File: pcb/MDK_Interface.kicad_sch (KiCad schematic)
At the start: 14 parts, among them J1 GROVE-CONNECTOR-DIP_4P-2.0_, J10 Conn_01x02, J11 Conn_01x02, J2 GROVE-CONNECTOR-DIP-90D_4P-2.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, J3 GROVE-CONNECTOR-DIP_4P-2.0_, J4 GROVE-CONNECTOR-DIP_4P-2.0_, J5 GROVE-CONNECTOR-DIP_4P-2.0_, J6 GROVE-CONNECTOR-DIP_4P-2.0_, J7 seeed:GROVE-HW4-2.0, J8 GROVE-CONNECTOR-SMD_4+2P-2.0_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

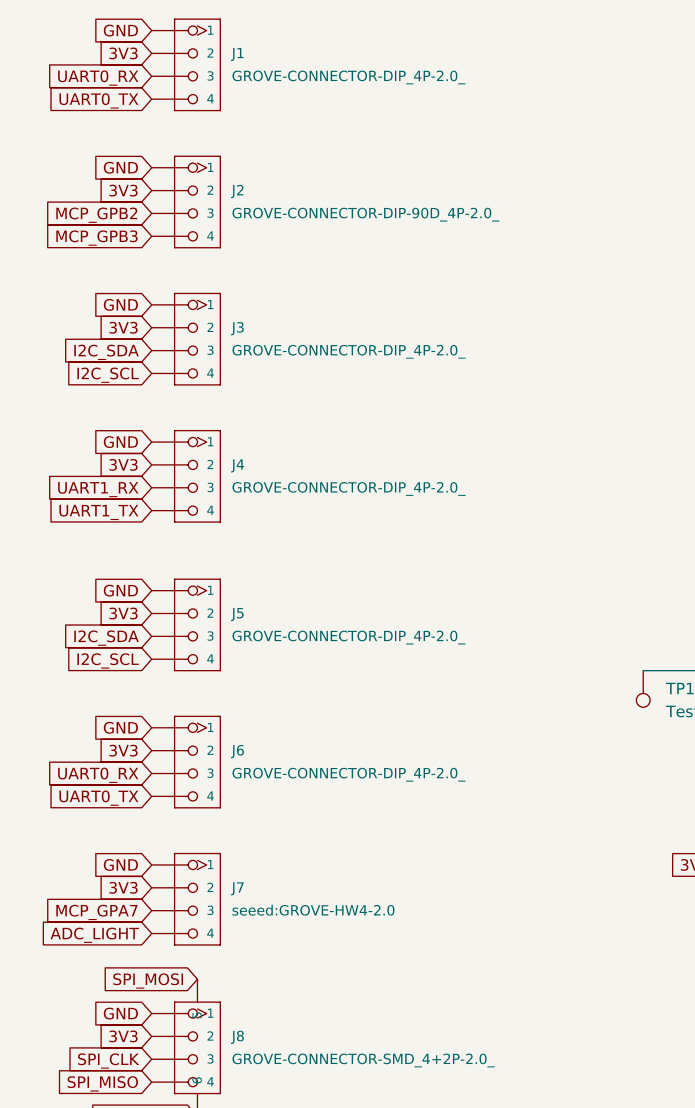
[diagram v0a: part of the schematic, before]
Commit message: adds grove connectors fix and rerouting
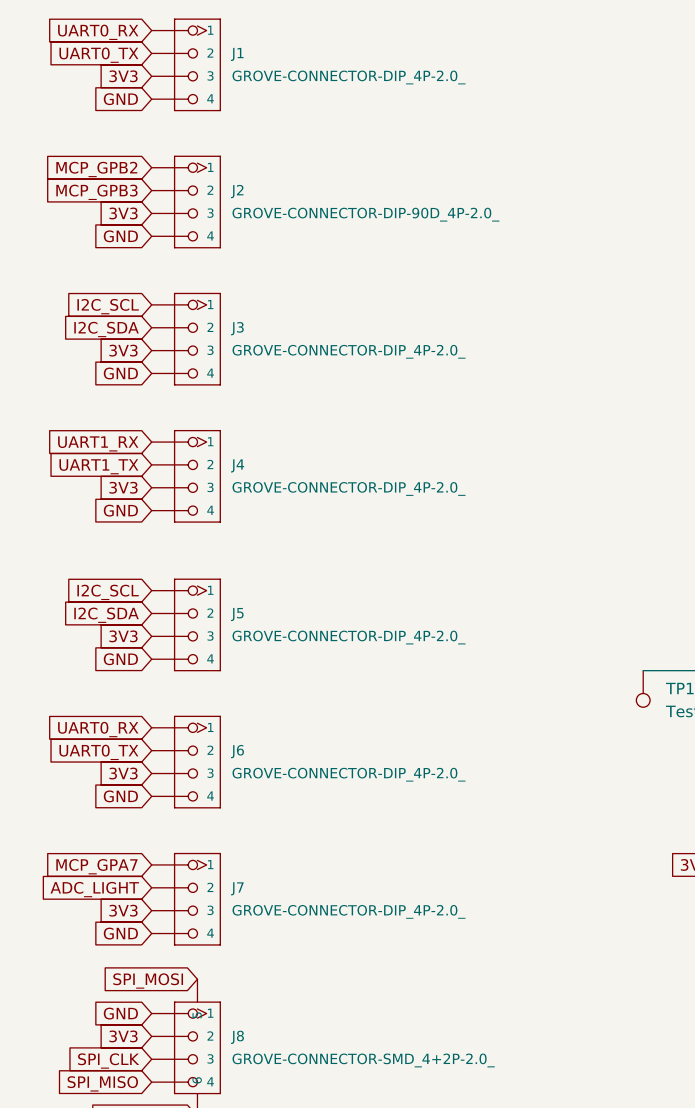
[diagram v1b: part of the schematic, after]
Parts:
- J7: value seeed:GROVE-HW4-2.0 -> GROVE-CONNECTOR-DIP_4P-2.0_
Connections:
- net 3V3: now also J1.3, J2.3, J3.3, J4.3, J5.3, J6.3, J7.3; no longer J1.2, J2.2, J3.2, J4.2, J5.2, J6.2, J7.2
- net ADC_LIGHT: now also J7.2; no longer J7.4
- net GND: now also J1.4, J2.4, J3.4, J4.4, J5.4, J6.4, J7.4; no longer J1.1, J2.1, J3.1, J4.1, J5.1, J6.1, J7.1
- net I2C_SCL: now also J3.1, J5.1; no longer J3.4, J5.4
- net I2C_SDA: now also J3.2, J5.2; no longer J3.3, J5.3
- net MCP_GPA7: now also J7.1; no longer J7.3
- net MCP_GPB2: now also J2.1; no longer J2.3
- net MCP_GPB3: now also J2.2; no longer J2.4
- net UART0_RX: now also J1.1, J6.1; no longer J1.3, J6.3
- net UART0_TX: now also J1.2, J6.2; no longer J1.4, J6.4
- net UART1_RX: now also J4.1; no longer J4.3
- net UART1_TX: now also J4.2; no longer J4.4
